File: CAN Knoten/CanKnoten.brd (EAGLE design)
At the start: 112.9 x 61.3 mm, 46 parts, among them IC1 74LS165D, K1 68711614522, K2 68711614522, K3 68711614522, K4 68711614522, Q1 HC49-U - 16MHz, Q2 HC49-U - xMHz, X1 MSTBV3

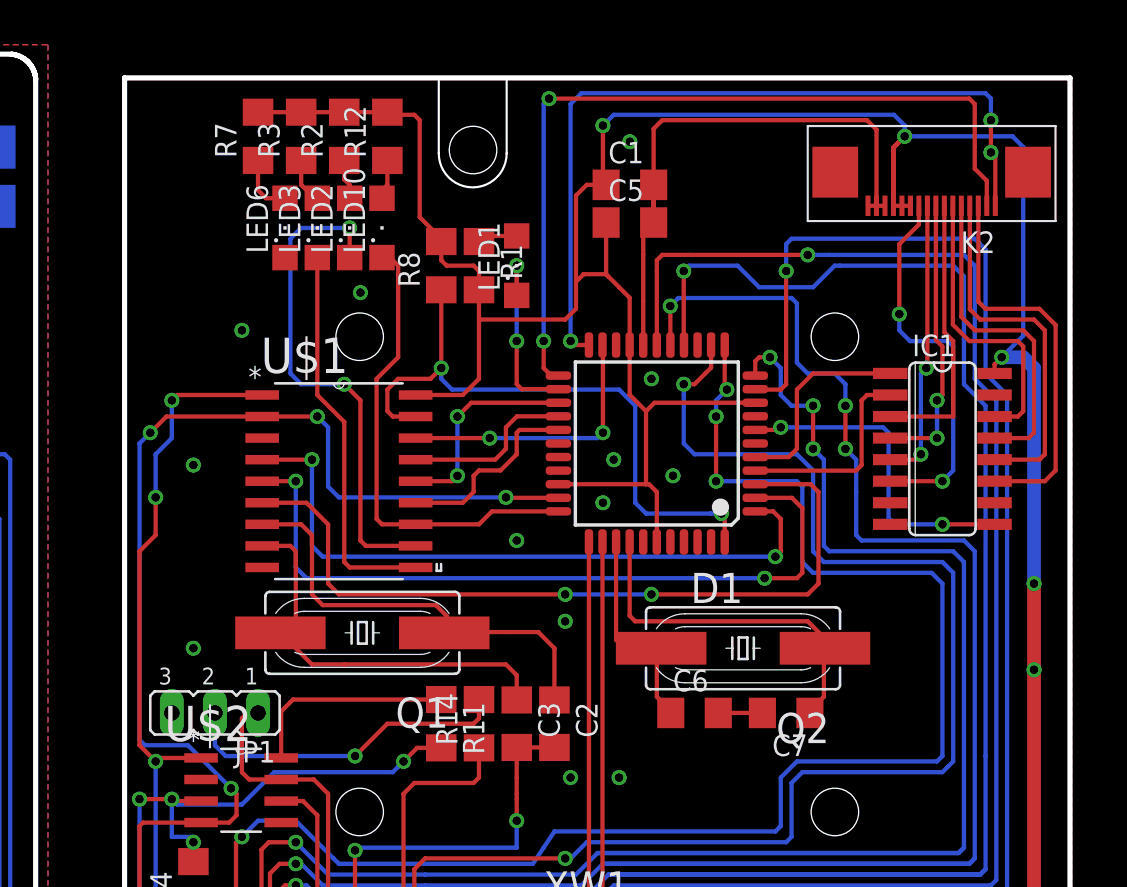
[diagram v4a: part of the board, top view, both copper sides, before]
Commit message: 
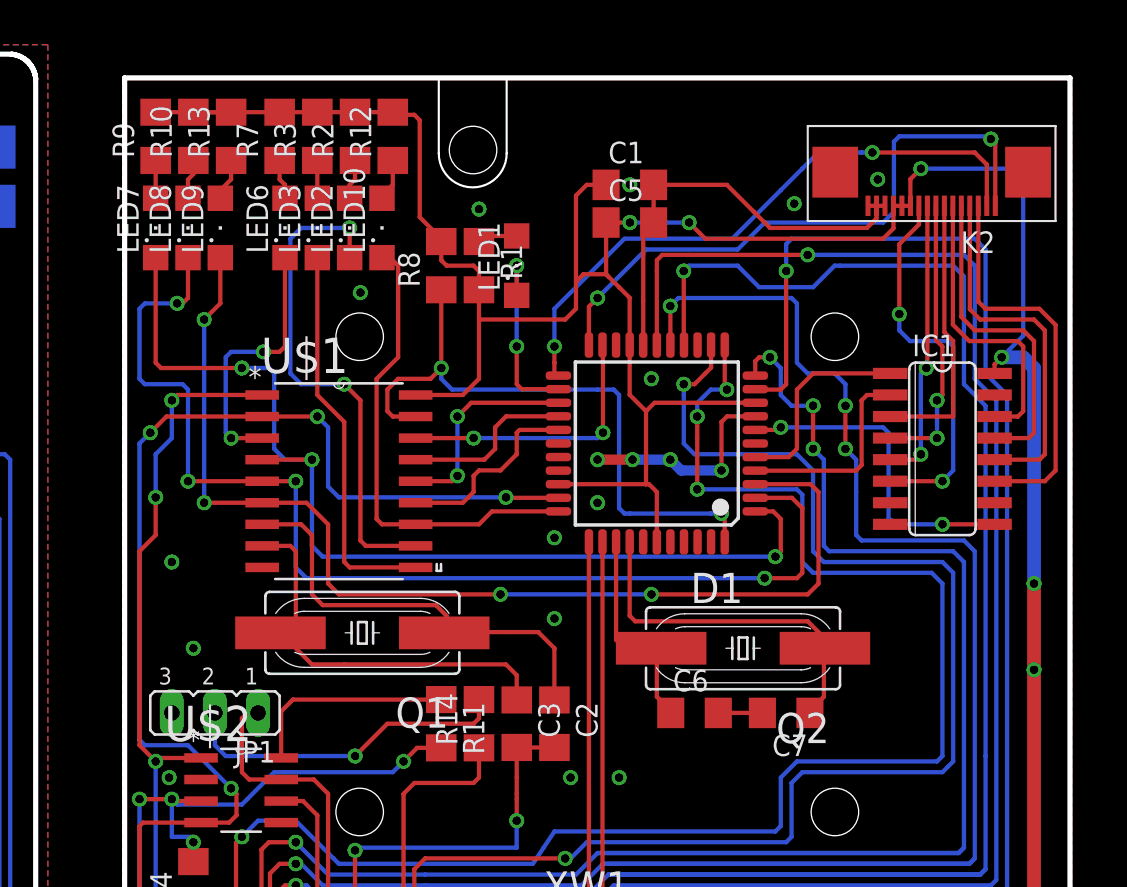
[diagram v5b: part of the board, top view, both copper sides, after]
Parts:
- added LED7, LED8, LED9: (no value), led:SML1206
- added R10, R13, R9: 560R, rcl:R1206
- moved R7 1.27 mm to (55.9, 14.9)
- moved R3 0.95 mm to (58.1, 14.9)
- moved R2 0.64 mm to (60.3, 14.9)
- moved R12 0.32 mm to (62.5, 14.9)
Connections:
- new net N$14: LED7.A, R9.1
- new net N$17: LED8.A, R10.1
- new net N$18: LED9.A, R13.1
- net MCP2515_TX0RTS: now also LED7.C
- net MCP2515_TX1RTS: now also LED8.C
- net MCP2515_TX2RTS: now also LED9.C
- net VCC: now also R10.2, R13.2, R9.2
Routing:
- net MCP2515_TX1RTS: track 44.1 -> 66.6 mm, vias 2 -> 4
- net MCP2515_TX0RTS: track 39.6 -> 60.0 mm, vias 2 -> 3
- net MCP2515_TX2RTS: track 46.6 -> 64.9 mm, vias 2 -> 4
- net MCP2515_CLKOUT: track 0.00 -> 15.9 mm, vias 0 -> 2
- net DEBUG_TXD: track 48.6 -> 36.1 mm
- net DEBUG_RXD: track 46.7 -> 36.9 mm, vias 3 -> 2
- net GND: track 62.9 -> 67.5 mm, vias 16 -> 21
- net VCC: track 301.5 -> 298.7 mm, vias 15 -> 16
- net N$18: track 0.00 -> 2.49 mm
- net N$17: track 0.00 -> 2.36 mm
- net N$14: track 0.00 -> 2.23 mm
- net EXTENDED_UART_RXD: track 91.0 -> 93.2 mm
- net N$13: track 3.54 -> 2.36 mm
- net MCP2515_RESET: track 36.9 -> 37.5 mm

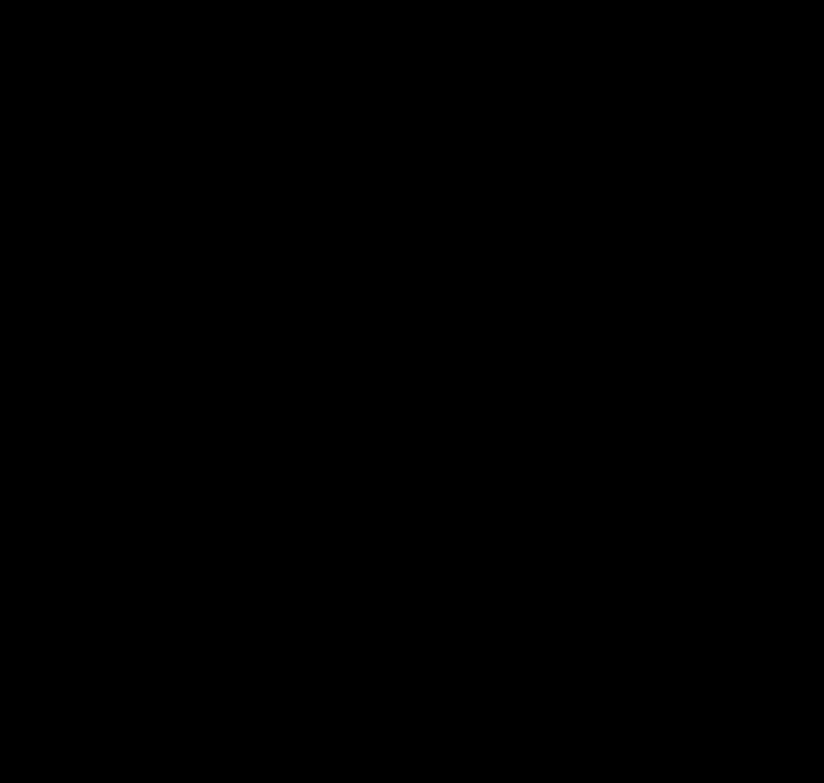
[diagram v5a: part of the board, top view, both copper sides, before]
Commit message: 
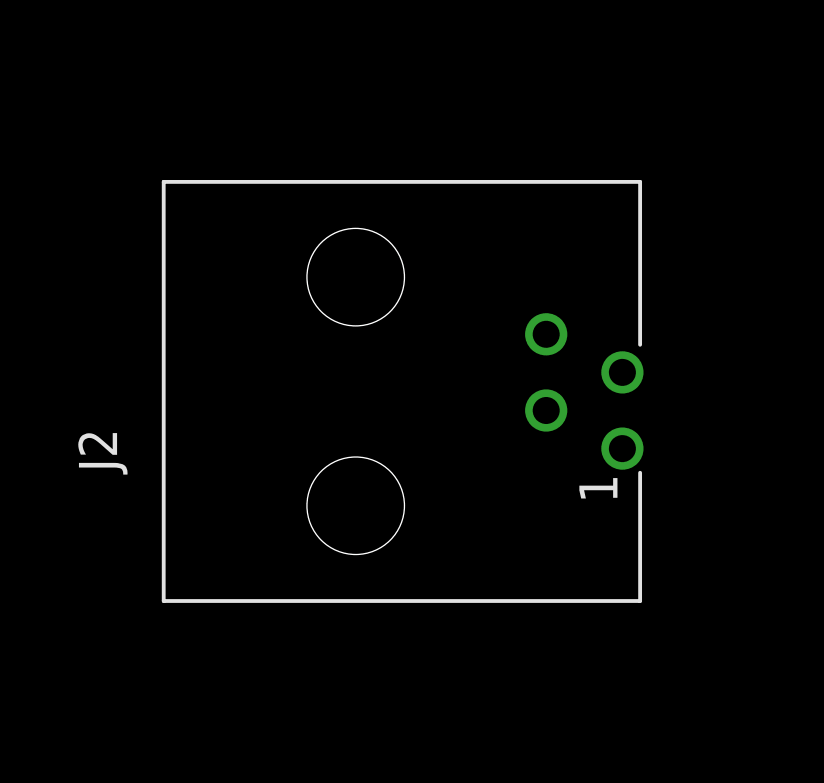
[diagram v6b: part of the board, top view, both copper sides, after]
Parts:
- added J2: (no value), InputOutputIO (rev18b):615004144021
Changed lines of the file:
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@@
 <element name="LED9" library="led" package="SML1206" value="" x="52.3875" y="9.525" rot="R90"/>
 <element name="R13" library="rcl" package="R1206" value="560R" x="53.0225" y="14.9225" rot="R90"/>
+<element name="J2" library="InputOutputIO (rev18b)" package="615004144021" value="" x="7.9375" y="-11.43" rot="R90"/>
 </elements>
 <signals>
